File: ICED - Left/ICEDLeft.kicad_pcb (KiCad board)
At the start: 2 copper layers, 176.2 x 145.8 mm, 165 parts, among them P1 Conn_ARM_JTAG_SWD_10, P2 DX07S024XJ1R1100, P3 CONN_17, P4 692121130100, P5 RGB Out, Q1 TC1264, U1 MK20DX256VLH7, U2 IS31FL3737-QFLS4-TR, X1 NX3225SA-16.000MHZ-STD-CSR-

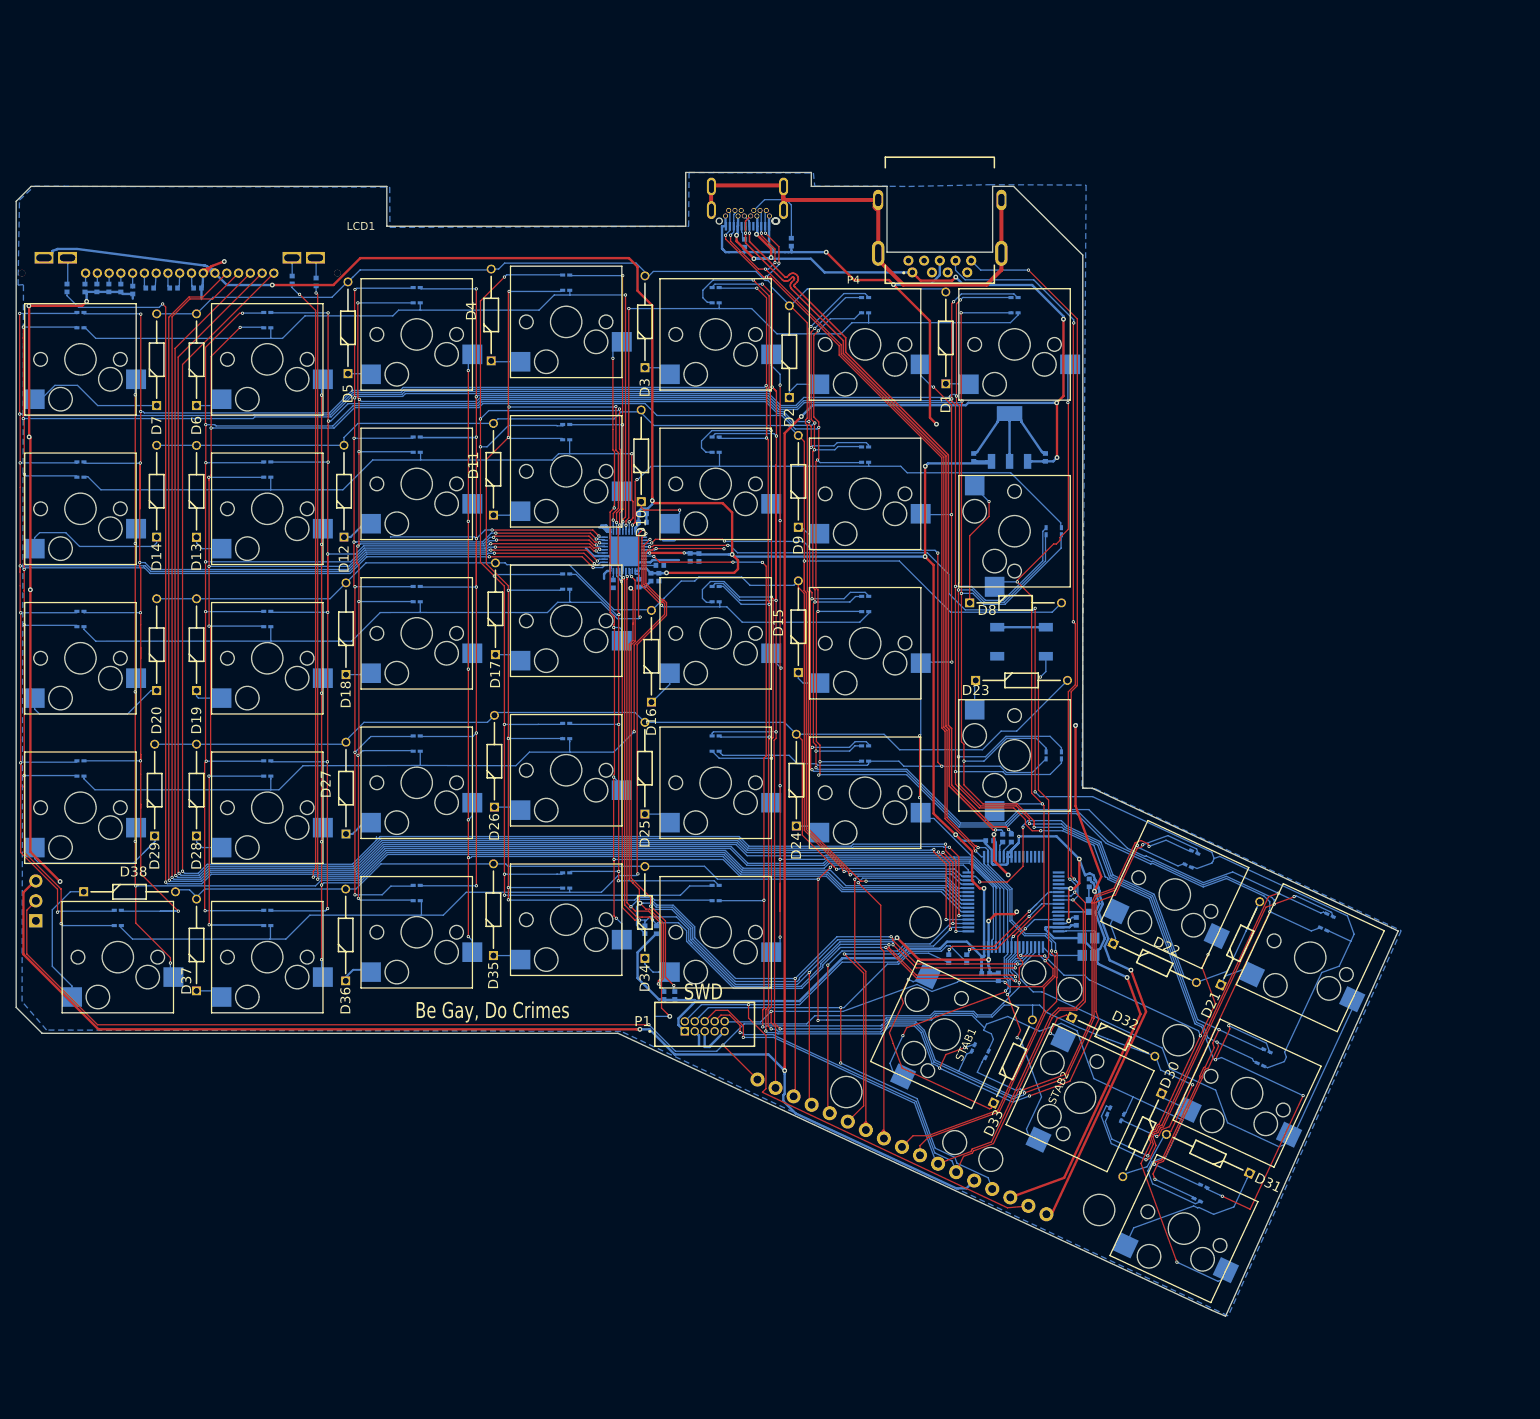
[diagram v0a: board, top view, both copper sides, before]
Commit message: set jcl design constraints
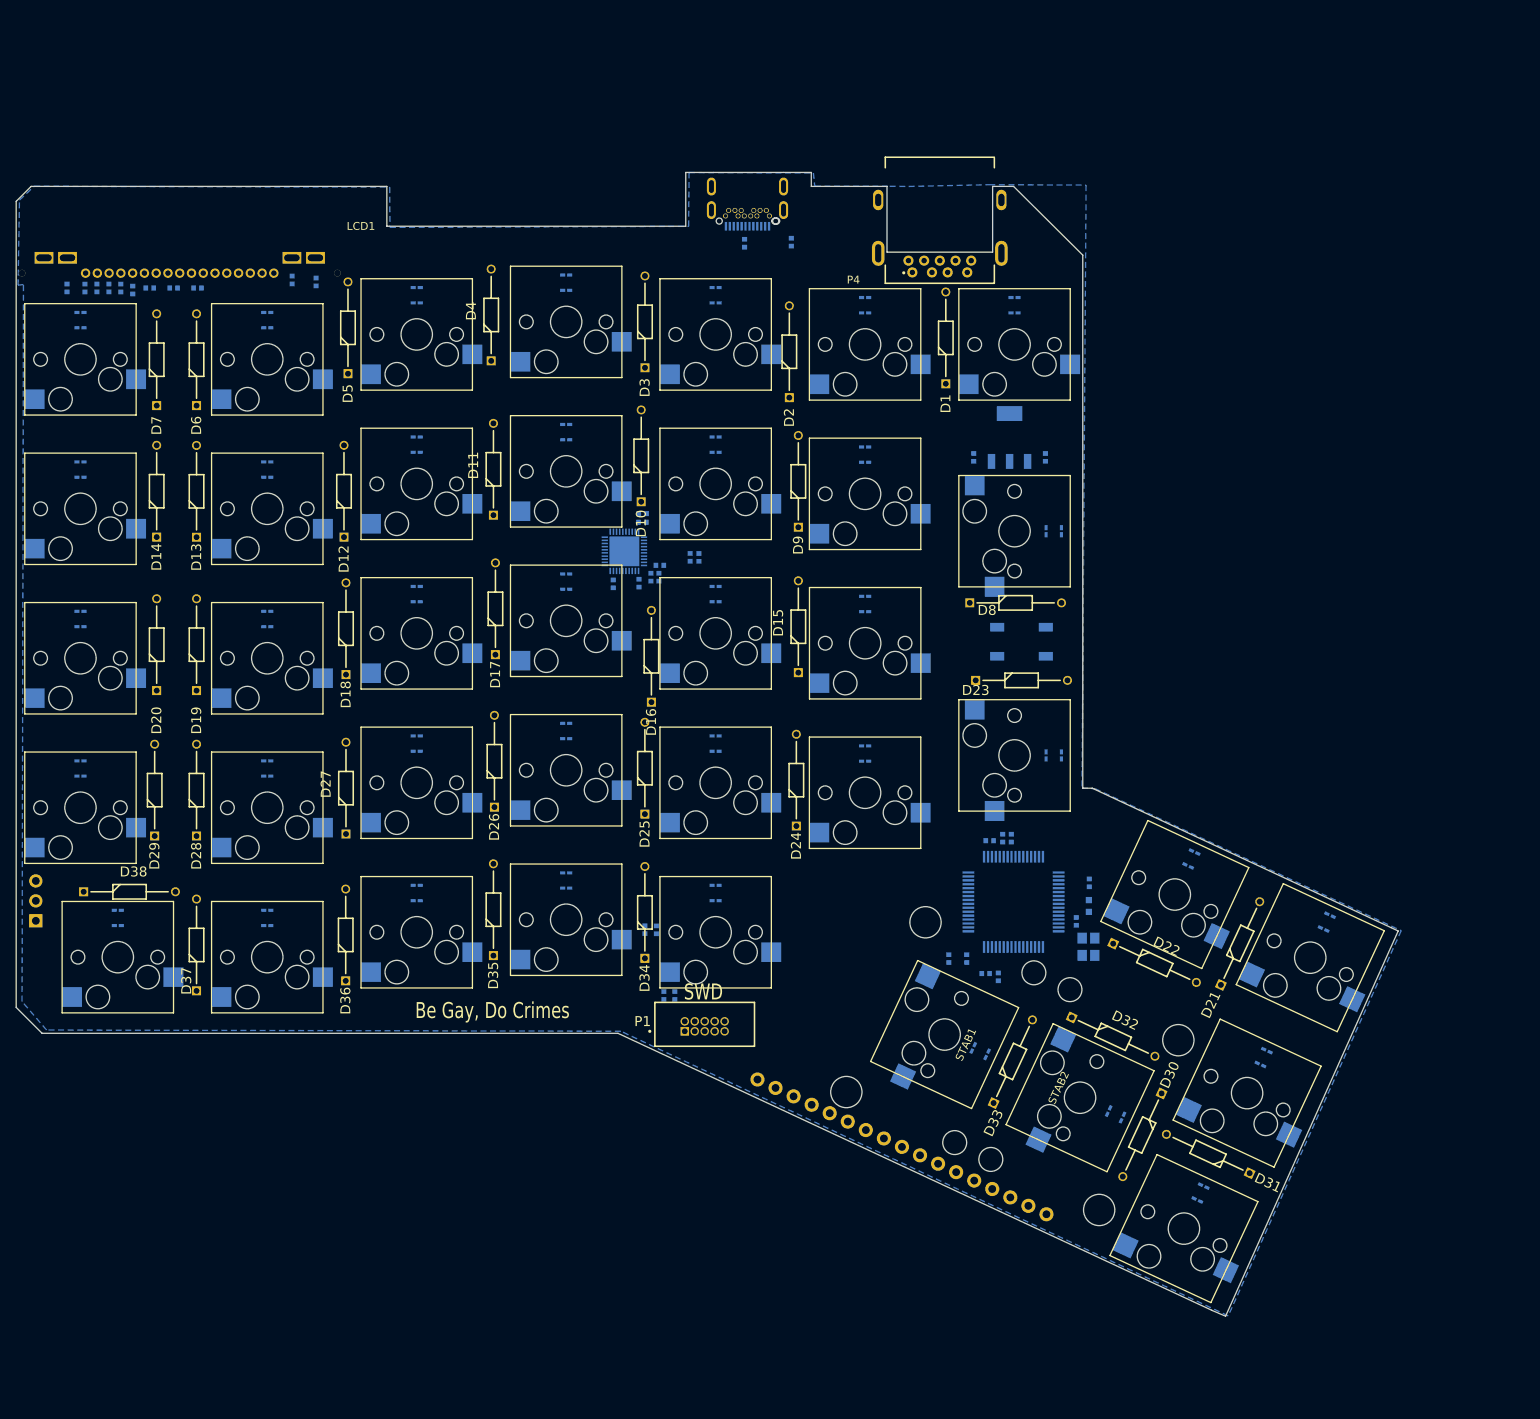
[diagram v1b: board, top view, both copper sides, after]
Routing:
- net /mcu/ledmatrix_2/Green1: track 524.9 -> 0.00 mm, vias 17 -> 0
- net /mcu/ledmatrix_2/Red1: track 515.8 -> 0.00 mm, vias 17 -> 0
- net /mcu/ledmatrix_2/Blue1: track 486.6 -> 0.00 mm, vias 19 -> 0
- net VSS: track 460.4 -> 0.00 mm, vias 21 -> 0
- net /mcu/ledmatrix_2/Green2: track 446.7 -> 0.00 mm, vias 17 -> 0
- net /mcu/ledmatrix_2/Blue2: track 434.8 -> 0.00 mm, vias 18 -> 0
- net /mcu/ledmatrix_2/Red2: track 433.0 -> 0.00 mm, vias 17 -> 0
- net VDD: track 422.1 -> 0.00 mm, vias 15 -> 0
- net /mcu/ledmatrix_2/Green3: track 412.3 -> 0.00 mm, vias 16 -> 0
- net /mcu/ledmatrix_2/Blue3: track 411.5 -> 0.00 mm, vias 18 -> 0
- net /mcu/ledmatrix_2/Red3: track 403.8 -> 0.00 mm, vias 16 -> 0
- net +5V: track 342.5 -> 0.00 mm, vias 11 -> 0
- net /mcu/SCLK: track 233.5 -> 0.00 mm, vias 4 -> 0
- net /mcu/MOSI: track 231.6 -> 0.00 mm, vias 4 -> 0
- net /Row4: track 227.7 -> 0.00 mm, vias 3 -> 0
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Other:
- net class 4mil removed
- net class Default removed
- net class GND removed
- net class Power removed

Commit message: No DRC violations!
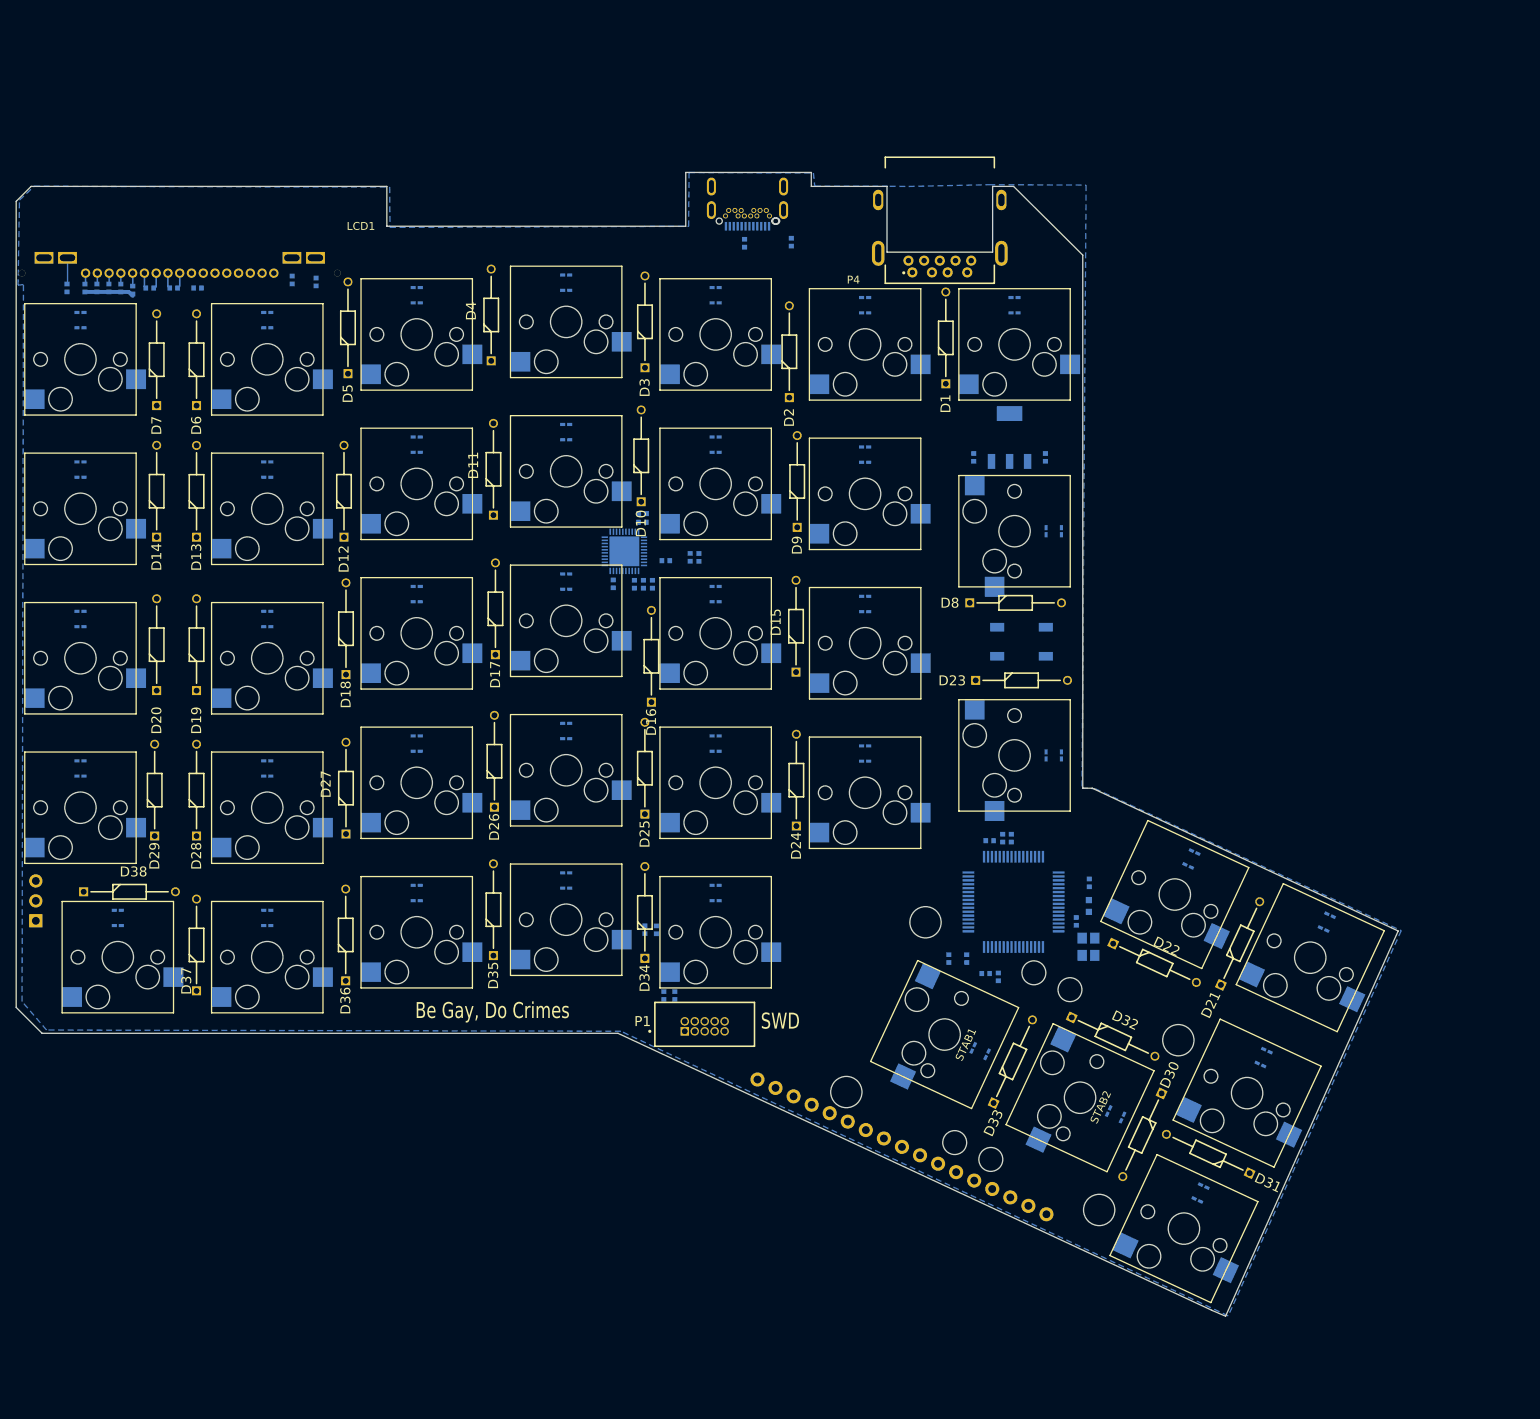
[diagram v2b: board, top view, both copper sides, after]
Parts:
- P5: footprint Connector_PinHeader_2.54mm:PinHeader_1x03_P2.54mm_Horizontal -> Connector_PinHeader_2.54mm:PinHeader_1x03_P2.54mm_Vertical
- moved C9 1.31 mm to (85.5, 105.9)
- moved C20 1.21 mm to (86.6, 105.9)
- moved R12 0.96 mm to (88.3, 102.9)
- moved C21 0.59 mm to (84.3, 105.9)
- moved D15 0.30 mm to (104.9, 117.1)
- moved D9 0.14 mm to (105.0, 98.7)
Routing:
- net VSS: track 0.00 -> 6.30 mm
- net Net-(LCD1-Pad2): track 0.00 -> 3.25 mm
- net Net-(C11-Pad2): track 0.00 -> 2.13 mm
- net Net-(C12-Pad1): track 0.00 -> 2.05 mm
- net Net-(C12-Pad2): track 0.00 -> 1.97 mm
- net Net-(C11-Pad1): track 0.00 -> 1.71 mm
- net Net-(C13-Pad2): track 0.00 -> 1.61 mm
- net Net-(C15-Pad2): track 0.00 -> 1.35 mm
- net Net-(C14-Pad2): track 0.00 -> 1.31 mm
- net Net-(C17-Pad2): track 0.00 -> 1.30 mm
- net Net-(C16-Pad2): track 0.00 -> 1.21 mm

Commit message: Routing WIP
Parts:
- moved R7 11.8 mm to (115.0, 155.8)
- moved R6 10.9 mm to (113.7, 155.8)
- moved D34 3.64 mm to (85.2, 157.2)
- moved C3 3.54 mm to (131.9, 157.6)
- moved C5 3.47 mm to (133.6, 157.8)
- moved D35 3.37 mm to (66.3, 156.6)
- moved D17 2.56 mm to (66.3, 117.4)
- moved R14 2.01 mm to (96.5, 63.2)
- moved R2 1.50 mm to (133.4, 137.2)
- moved R1 1.43 mm to (132.3, 137.3)
- moved D38 1.19 mm to (12.9, 144.8)
- moved C4 1.09 mm to (129.6, 137.5)
- moved U1 0.79 mm to (132.7, 145.6)
- moved D16 0.57 mm to (85.9, 120.9)
- moved X1 0.27 mm to (142.1, 152.4)
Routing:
- net /mcu/LCD_KR: track 0.00 -> 208.4 mm, vias 0 -> 2
- net /mcu/RST: track 0.00 -> 196.7 mm, vias 0 -> 1
- net /Col9: track 0.00 -> 196.0 mm, vias 0 -> 6
- net /mcu/SCLK: track 0.00 -> 189.4 mm, vias 0 -> 1
- net /mcu/ledmatrix_2/Green1: track 0.00 -> 187.4 mm, vias 0 -> 6
- net /mcu/MOSI: track 0.00 -> 186.5 mm, vias 0 -> 1
- net /mcu/SS1: track 0.00 -> 185.1 mm, vias 0 -> 1
- net /mcu/A0: track 0.00 -> 184.5 mm, vias 0 -> 1
- net /mcu/ledmatrix_2/Red1: track 0.00 -> 184.0 mm, vias 0 -> 6
- net /mcu/LCD_KG: track 0.00 -> 171.7 mm, vias 0 -> 2
- net /Col8: track 0.00 -> 168.4 mm, vias 0 -> 6
- net /mcu/LCD_KB: track 0.00 -> 168.2 mm, vias 0 -> 2
- net /mcu/ledmatrix_2/Blue1: track 0.00 -> 166.7 mm, vias 0 -> 6
- net /mcu/ledmatrix_2/Red2: track 0.00 -> 159.5 mm, vias 0 -> 6
- net /mcu/ledmatrix_2/Green2: track 0.00 -> 154.6 mm, vias 0 -> 6
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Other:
- outline, holes or cut-outs redrawn

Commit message: Routing WIP2
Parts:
- moved R8 1.17 mm to (80.6, 105.2), turned to -90 degrees
- moved R14 0.95 mm to (97.5, 63.3)
- moved R12 0.85 mm to (88.0, 103.7), turned to 0 degrees
- moved D34 0.60 mm to (85.2, 157.8)
- moved D12 0.55 mm to (47.6, 100.3)
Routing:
- net /mcu/ledmatrix_2/Red1: track 184.0 -> 394.4 mm, vias 6 -> 12
- net /mcu/ledmatrix_2/Green1: track 187.4 -> 396.1 mm, vias 6 -> 12
- net /mcu/ledmatrix_2/Blue1: track 166.7 -> 369.9 mm, vias 6 -> 12
- net /mcu/ledmatrix_2/Blue2: track 143.4 -> 311.7 mm, vias 6 -> 13
- net /mcu/ledmatrix_2/Red2: track 159.5 -> 323.6 mm, vias 6 -> 11
- net /mcu/ledmatrix_2/Green2: track 154.6 -> 314.1 mm, vias 6 -> 12
- net /Row4: track 1.20 -> 150.1 mm, vias 0 -> 2
- net VDD: track 0.00 -> 145.9 mm, vias 0 -> 3
- net /Row3: track 2.86 -> 146.4 mm, vias 0 -> 2
- net /Col4: track 0.00 -> 104.5 mm, vias 0 -> 5
- net /mcu/ledmatrix_2/Row4B: track 0.00 -> 88.1 mm, vias 0 -> 2
- net /Row1: track 111.0 -> 196.1 mm, vias 0 -> 2
- net /mcu/ledmatrix_2/Red3: track 140.4 -> 220.7 mm, vias 6 -> 7
- net /mcu/ledmatrix_2/Green3: track 136.4 -> 214.3 mm
- net VSS: track 6.30 -> 70.1 mm, vias 0 -> 5
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
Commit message: 50 nets to go
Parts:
- moved R4 40.3 mm to (117.8, 125.7)
- moved R16 39.2 mm to (119.4, 127.7)
- moved R3 22.6 mm to (108.6, 148.9), turned to 0 degrees
- moved R5 20.7 mm to (107.3, 147.8)
- moved R7 13.7 mm to (103.2, 162.6), turned to 90 degrees
- moved R6 13.2 mm to (103.2, 163.8), turned to 90 degrees
- moved C5 5.55 mm to (138.7, 155.6), turned to 180 degrees
- moved D1 4.72 mm to (124.5, 85.0)
- moved C3 4.71 mm to (127.8, 155.4), turned to 90 degrees
- moved S34 3.98 mm to (95.1, 154.2)
- moved X1 3.98 mm to (142.6, 156.3)
- moved S11 3.98 mm to (76.1, 95.5)
- moved LED17 3.98 mm to (76.1, 109.5)
- moved D7 3.98 mm to (23.9, 87.1)
- moved D8 3.98 mm to (127.5, 112.2)
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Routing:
- net VDD: track 145.9 -> 381.6 mm, vias 3 -> 8
- net +5V: track 157.9 -> 338.4 mm, vias 3 -> 5
- net /mcu/ledmatrix_2/Row4C: track 8.89 -> 160.5 mm, vias 0 -> 4
- net /mcu/SDA0: track 9.83 -> 133.1 mm, vias 1 -> 6
- net /mcu/SCL0: track 9.94 -> 129.9 mm, vias 1 -> 7
- net /mcu/RGBOUT: track 0.00 -> 109.1 mm
- net /mcu/ledmatrix_2/Blue1: track 369.9 -> 465.4 mm, vias 12 -> 14
- net /mcu/ledmatrix_2/Green1: track 396.1 -> 487.5 mm, vias 12 -> 14
- net /mcu/ledmatrix_2/Red1: track 394.4 -> 480.8 mm, vias 12 -> 14
- net /mcu/ledmatrix_2/Green2: track 314.1 -> 395.0 mm, vias 12 -> 15
- net /mcu/ledmatrix_2/Blue2: track 311.7 -> 391.5 mm, vias 13 -> 15
- net /Col2: track 0.00 -> 79.2 mm, vias 0 -> 3
- net /mcu/ledmatrix_2/Blue3: track 188.3 -> 267.4 mm, vias 7 -> 10
- net /mcu/ledmatrix_2/Row5A: track 57.6 -> 133.4 mm, vias 2 -> 3
- net /mcu/ledmatrix_2/Red2: track 323.6 -> 397.7 mm, vias 11 -> 14
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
